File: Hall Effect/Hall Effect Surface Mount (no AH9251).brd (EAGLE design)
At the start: 34 x 25.4 mm, 6 parts

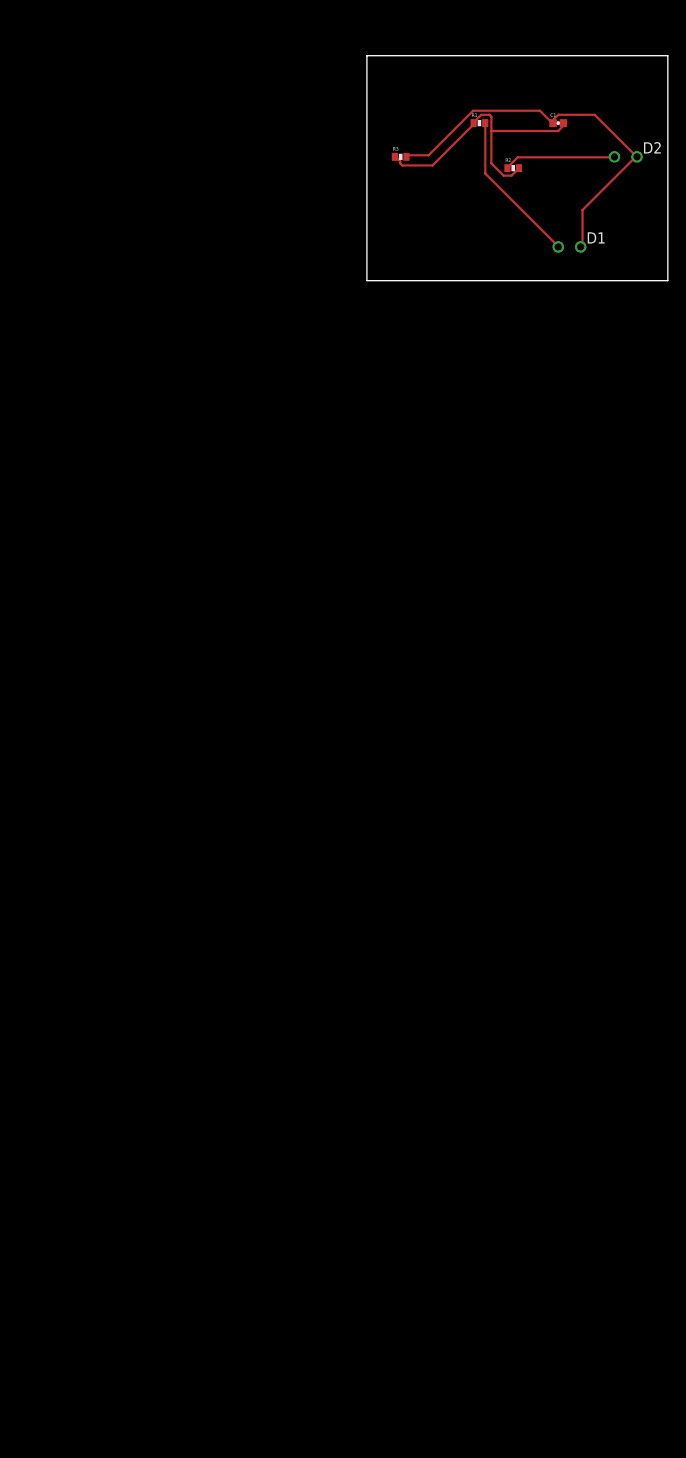
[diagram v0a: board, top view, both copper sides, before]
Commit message: Completed schematic with correct part for sensor. Added component values
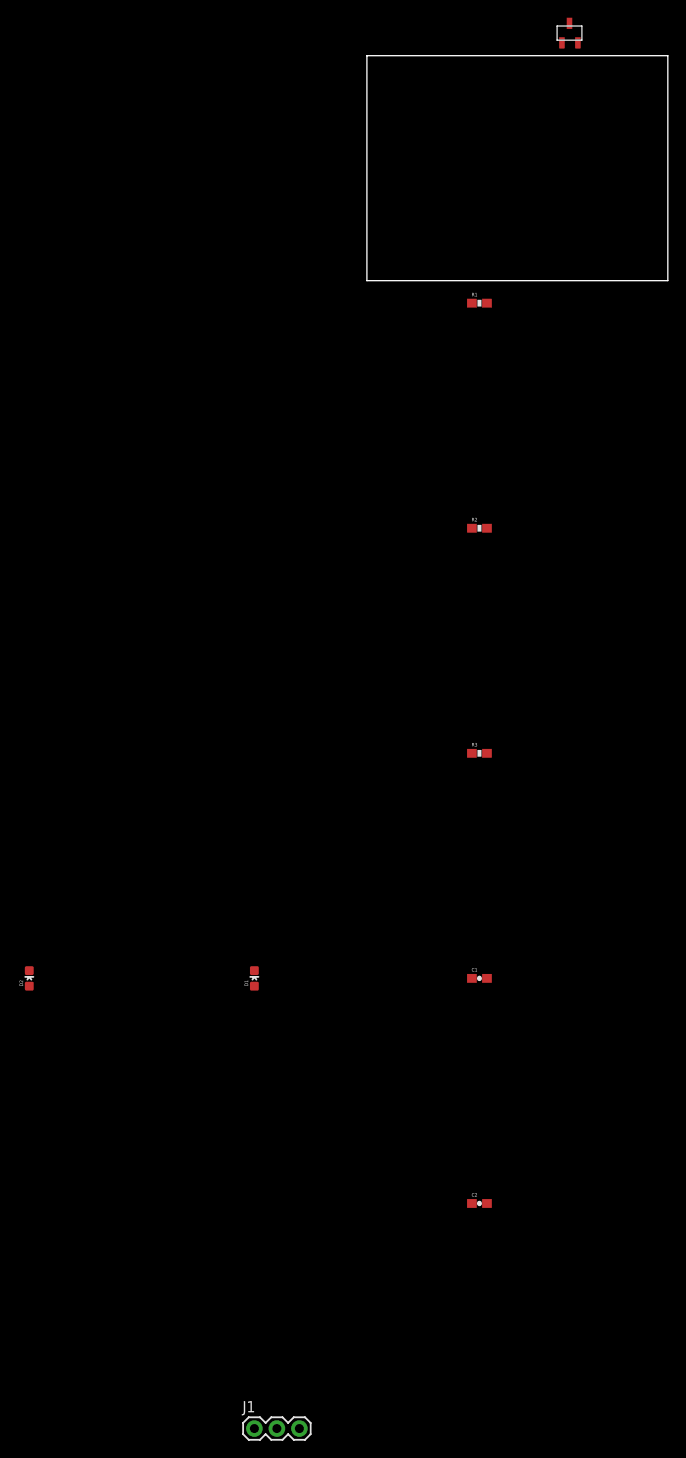
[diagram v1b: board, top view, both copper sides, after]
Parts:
- added C2: 4.7nF, SparkFun-Passives:0603-CAP
- added J1: (no value), SparkFun-Connectors:1X03
- added U$1: US5881-HALL-EFFECT, TPS5430:US5881-HALL-EFFECT
- C1: value (none) -> 0.1uF; device SparkFun-Capacitors:0402-CAP -> SparkFun-Passives:0603-CAP
- D1: value (none) -> Power; device SparkFun-LED:LED3MM-NS -> SparkFun-LED:LED-0603
- D2: value (none) -> Signal; device SparkFun-LED:LED3MM-NS -> SparkFun-LED:LED-0603
- R1, R3: value (none) -> 2k; device SparkFun-Passives:0402-RES -> SparkFun-Passives:0603-RES
- R2: value (none) -> 10k; device SparkFun-Passives:0402-RES -> SparkFun-Passives:0603-RES
- moved D2 114.6 mm to (-25.4, -76.2)
- moved C1 96.9 mm to (25.4, -76.2)
- moved D1 89.9 mm to (0.00, -76.2)
- moved R3 67.9 mm to (25.4, -50.8)
- moved R2 40.8 mm to (25.4, -25.4)
- moved R1 20.3 mm to (25.4, 0.00)
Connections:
- new net N$3: C2.2, D2.C, J1.1, R2.2, U$1.VOUT
- net GND: now also C1.2, C2.1, D1.C, J1.3, U$1.GND; no longer C1.1, D1.K, D2.K, R3.2
- net N$2: now also R3.1; no longer R2.1
- net VCC: now also C1.1, J1.2, R2.1, R3.2, U$1.VDD; no longer C1.2, R2.2, R3.1
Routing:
- net GND: track 44.3 -> 0.00 mm
- net VCC: track 32.0 -> 0.00 mm
- net N$1: track 17.4 -> 0.00 mm
- net N$2: track 12.6 -> 0.00 mm
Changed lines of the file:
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@@
 <?xml version="1.0" encoding="utf-8"?>
 <!DOCTYPE eagle SYSTEM "eagle.dtd">
-<eagle version="7.6.0">
+<eagle version="7.1.0">
 <drawing>
 <settings>
@@
 <setting verticaltext="up"/>
 </settings>
-<grid distance="0.05" unitdist="inch" unit="inch" style="lines" multiple="1" display="no" altdistance="0.025" altunitdist="inch" altunit="inch"/>
+<grid distance="1" unitdist="inch" unit="inch" style="lines" multiple="1" display="yes" altdistance="0.025" altunitdist="inch" altunit="inch"/>
 <layers>
 <layer number="1" name="Top" color="4" fill="1" visible="yes" active="yes"/>
@@
 <layer number="112" name="tSilk" color="7" fill="1" visible="yes" active="yes"/>
 <layer number="113" name="IDFDebug" color="4" fill="1" visible="yes" active="yes"/>
+<layer number="114" name="Badge_Outline" color="7" fill="1" visible="yes" active="yes"/>
+<layer number="115" name="ReferenceISLANDS" color="7" fill="1" visible="yes" active="yes"/>
 <layer number="116" name="Patch_BOT" color="9" fill="4" visible="yes" active="yes"/>
 <layer number="118" name="Rect_Pads" color="7" fill="1" visible="yes" active="yes"/>
@@
 </autorouter>
 <elements>
-<element name="C1" library="SparkFun-Capacitors" package="0402-CAP" value="" x="34.29" y="20.32"/>
-<element name="D1" library="SparkFun-LED" package="LED3MM-NS" value="" x="35.56" y="6.35"/>
-<element name="D2" library="SparkFun-LED" package="LED3MM-NS" value="" x="41.91" y="16.51"/>
-<element name="R1" library="SparkFun-Passives" package="0402-RES" value="" x="25.4" y="20.32"/>
-<element name="R2" library="SparkFun-Passives" package="0402-RES" value="" x="29.21" y="15.24"/>
-<element name="R3" library="SparkFun-Passives" package="0402-RES" value="" x="16.51" y="16.51"/>
+<element name="U$1" library="TPS5430" package="US5881-HALL-EFFECT" value="US5881-HALL-EFFECT" x="35.56" y="30.48"/>
+<element name="R1" library="SparkFun-Passives" package="0603-RES" value="2k" x="25.4" y="0"/>
+<element name="R2" library="SparkFun-Passives" package="0603-RES" value="10k" x="25.4" y="-25.4"/>
+<element name="R3" library="SparkFun-Passives" package="0603-RES" value="2k" x="25.4" y="-50.8"/>
+<element name="C1" library="SparkFun-Passives" package="0603-CAP" value="0.1uF" x="25.4" y="-76.2"/>
+<element name="C2" library="SparkFun-Passives" package="0603-CAP" value="4.7nF" x="25.4" y="-101.6"/>
+<element name="D1" library="SparkFun-LED" package="LED-0603" value="Power" x="0" y="-76.2"/>
+<element name="D2" library="SparkFun-LED" package="LED-0603" value="Signal" x="-25.4" y="-76.2"/>
+<element name="J1" library="SparkFun-Connectors" package="1X03" value="" x="0" y="-127"/>
 </elements>
 <signals>
 <signal name="VCC">
 <contactref element="R1" pad="1"/>
-<contactref element="C1" pad="2"/>
-<contactref element="R3" pad="1"/>
-<contactref element="R2" pad="2"/>
-<wire x1="29.0322" y1="14.4018" x2="29.718" y2="15.0876" width="0.254" layer="1"/>
-<wire x1="28.1178" y1="14.4018" x2="29.0322" y2="14.4018" width="0.254" layer="1"/>
-<wire x1="26.7462" y1="15.7734" x2="28.1178" y2="14.4018" width="0.254" layer="1"/>
-<wire x1="26.7462" y1="21.0312" x2="26.7462" y2="19.431" width="0.254" layer="1"/>
-<wire x1="26.7462" y1="19.431" x2="26.7462" y2="15.7734" width="0.254" layer="1"/>
-<wire x1="26.5176" y1="21.2598" x2="26.7462" y2="21.0312" width="0.254" layer="1"/>
-<wire x1="25.6032" y1="21.2598" x2="26.5176" y2="21.2598" width="0.254" layer="1"/>
-<wire x1="24.6888" y1="20.3454" x2="25.6032" y2="21.2598" width="0.254" layer="1"/>
-<wire x1="29.718" y1="15.0876" x2="29.86" y2="15.24" width="0.254" layer="1"/>
-<wire x1="24.6888" y1="20.3454" x2="24.75" y2="20.32" width="0.254" layer="1"/>
-<wire x1="16.4592" y1="16.002" x2="16.002" y2="16.4592" width="0.254" layer="1"/>
-<wire x1="16.4592" y1="15.7734" x2="16.4592" y2="16.002" width="0.254" layer="1"/>
-<wire x1="16.6878" y1="15.5448" x2="16.4592" y2="15.7734" width="0.254" layer="1"/>
-<wire x1="20.1168" y1="15.5448" x2="16.6878" y2="15.5448" width="0.254" layer="1"/>
-<wire x1="24.6888" y1="20.1168" x2="20.1168" y2="15.5448" width="0.254" layer="1"/>
-<wire x1="16.002" y1="16.4592" x2="15.86" y2="16.51" width="0.254" layer="1"/>
-<wire x1="24.6888" y1="20.1168" x2="24.75" y2="20.32" width="0.254" layer="1"/>
-<wire x1="34.7472" y1="19.8882" x2="34.7472" y2="20.1168" width="0.254" layer="1"/>
-<wire x1="34.29" y1="19.431" x2="34.7472" y2="19.8882" width="0.254" layer="1"/>
-<wire x1="26.7462" y1="19.431" x2="34.29" y2="19.431" width="0.254" layer="1"/>
-<wire x1="34.7472" y1="20.1168" x2="34.87" y2="20.32" width="0.254" layer="1"/>
+<contactref element="R2" pad="1"/>
+<contactref element="R3" pad="2"/>
+<contactref element="C1" pad="1"/>
+<contactref element="U$1" pad="VDD"/>
+<contactref element="J1" pad="2"/>
+<wire x1="24.55" y1="-76.2" x2="2.54" y2="-127" width="0" layer="19" extent="1-1"/>
+<wire x1="26.25" y1="-50.8" x2="24.55" y2="-76.2" width="0" layer="19" extent="1-1"/>
+<wire x1="24.55" y1="-25.4" x2="26.25" y2="-50.8" width="0" layer="19" extent="1-1"/>
+<wire x1="24.55" y1="0" x2="24.55" y2="-25.4" width="0" layer="19" extent="1-1"/>
+<wire x1="34.71" y1="29.38" x2="24.55" y2="0" width="0" layer="19" extent="1-1"/>
 </signal>
 <signal name="N$1">
 <contactref element="R1" pad="2"/>
 <contactref element="D1" pad="A"/>
-<wire x1="26.0604" y1="14.6304" x2="26.0604" y2="20.1168" width="0.254" layer="1"/>
-<wire x1="34.29" y1="6.4008" x2="26.0604" y2="14.6304" width="0.254" layer="1"/>
-<wire x1="26.0604" y1="20.1168" x2="26.05" y2="20.32" width="0.254" layer="1"/>
-<wire x1="34.29" y1="6.4008" x2="34.29" y2="6.35" width="0.254" layer="1"/>
+<wire x1="26.25" y1="0" x2="0" y2="-77.077" width="0" layer="19" extent="1-1"/>
+</signal>
+<signal name="N$2">
+<contactref element="R3" pad="1"/>
+<contactref element="D2" pad="A"/>
+<wire x1="24.55" y1="-50.8" x2="-25.4" y2="-77.077" width="0" layer="19" extent="1-1"/>
+</signal>
+<signal name="N$3">
+<contactref element="R2" pad="2"/>
+<contactref element="D2" pad="C"/>
+<contactref element="C2" pad="2"/>
+<contactref element="U$1" pad="VOUT"/>
+<contactref element="J1" pad="1"/>
+<wire x1="26.25" y1="-101.6" x2="0" y2="-127" width="0" layer="19" extent="1-1"/>
+<wire x1="-25.4" y1="-75.323" x2="0" y2="-127" width="0" layer="19" extent="1-1"/>
+<wire x1="26.25" y1="-25.4" x2="-25.4" y2="-75.323" width="0" layer="19" extent="1-1"/>
+<wire x1="36.51" y1="29.38" x2="26.25" y2="-25.4" width="0" layer="19" extent="1-1"/>
 </signal>
 <signal name="GND">
-<contactref element="R3" pad="2"/>
-<contactref element="C1" pad="1"/>
-<contactref element="D1" pad="K"/>
-<contactref element="D2" pad="K"/>
-<wire x1="19.6596" y1="16.6878" x2="17.3736" y2="16.6878" width="0.254" layer="1"/>
-<wire x1="24.6888" y1="21.717" x2="19.6596" y2="16.6878" width="0.254" layer="1"/>
-<wire x1="32.2326" y1="21.717" x2="24.6888" y2="21.717" width="0.254" layer="1"/>
-<wire x1="33.6042" y1="20.3454" x2="32.2326" y2="21.717" width="0.254" layer="1"/>
-<wire x1="17.3736" y1="16.6878" x2="17.16" y2="16.51" width="0.254" layer="1"/>
-<wire x1="33.6042" y1="20.3454" x2="33.71" y2="20.32" width="0.254" layer="1"/>
-<wire x1="37.0332" y1="10.5156" x2="37.0332" y2="6.4008" width="0.254" layer="1"/>
-<wire x1="42.9768" y1="16.4592" x2="37.0332" y2="10.5156" width="0.254" layer="1"/>
-<wire x1="37.0332" y1="6.4008" x2="36.83" y2="6.35" width="0.254" layer="1"/>
-<wire x1="42.9768" y1="16.4592" x2="43.18" y2="16.51" width="0.254" layer="1"/>
-<wire x1="33.8328" y1="20.8026" x2="33.8328" y2="20.3454" width="0.254" layer="1"/>
-<wire x1="34.29" y1="21.2598" x2="33.8328" y2="20.8026" width="0.254" layer="1"/>
-<wire x1="38.4048" y1="21.2598" x2="34.29" y2="21.2598" width="0.254" layer="1"/>
-<wire x1="42.9768" y1="16.6878" x2="38.4048" y2="21.2598" width="0.254" layer="1"/>
-<wire x1="33.8328" y1="20.3454" x2="33.71" y2="20.32" width="0.254" layer="1"/>
-<wire x1="42.9768" y1="16.6878" x2="43.18" y2="16.51" width="0.254" layer="1"/>
-</signal>
-<signal name="N$2">
-<contactref element="R2" pad="1"/>
-<contactref element="D2" pad="A"/>
-<wire x1="29.718" y1="16.4592" x2="28.575" y2="15.3162" width="0.254" layer="1"/>
-<wire x1="40.4622" y1="16.4592" x2="29.718" y2="16.4592" width="0.254" layer="1"/>
-<wire x1="28.575" y1="15.3162" x2="28.56" y2="15.24" width="0.254" layer="1"/>
-<wire x1="40.4622" y1="16.4592" x2="40.64" y2="16.51" width="0.254" layer="1"/>
+<contactref element="D1" pad="C"/>
+<contactref element="C1" pad="2"/>
+<contactref element="C2" pad="1"/>
+<contactref element="U$1" pad="GND"/>
+<contactref element="J1" pad="3"/>
+<wire x1="24.55" y1="-101.6" x2="5.08" y2="-127" width="0" layer="19" extent="1-1"/>
+<wire x1="26.25" y1="-76.2" x2="24.55" y2="-101.6" width="0" layer="19" extent="1-1"/>
+<wire x1="0" y1="-75.323" x2="26.25" y2="-76.2" width="0" layer="19" extent="1-1"/>
+<wire x1="35.56" y1="31.58" x2="26.25" y2="-76.2" width="0" layer="19" extent="1-1"/>
 </signal>
 </signals>

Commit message: Initial board design
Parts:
- moved J1 132.5 mm to (10.2, 5.08)
- moved C2 111.0 mm to (15.2, 8.89), turned to 180 degrees
- moved D2 95.6 mm to (6.35, 14.0)
- moved D1 92.2 mm to (19.1, 14.0)
- moved C1 86.4 mm to (10.2, 8.89)
- moved R3 62.7 mm to (6.35, 8.89), turned to 270 degrees
- moved R2 41.4 mm to (12.7, 14.0), turned to 180 degrees
- moved U$1 25.6 mm to (12.7, 19.1)
- moved R1 10.9 mm to (19.1, 8.89), turned to 90 degrees
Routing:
- net VCC: track 0.00 -> 49.1 mm
- net N$3: track 0.00 -> 26.9 mm
- net GND: track 0.00 -> 25.5 mm
- net N$1: track 0.00 -> 3.54 mm
- net N$2: track 0.00 -> 3.38 mm
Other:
- board size 34 x 25.4 mm -> 20.4 x 22.9 mm
- board text added: "+"
- board text added: "-"
- board text added: "Power"
- board text added: "S"
- board text added: "Signal"
